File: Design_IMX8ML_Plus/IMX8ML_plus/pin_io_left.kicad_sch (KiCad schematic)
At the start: 2 parts, among them J1 DF40C-100DP-0.4V_51_, J2 DF40C-100DP-0.4V_51_

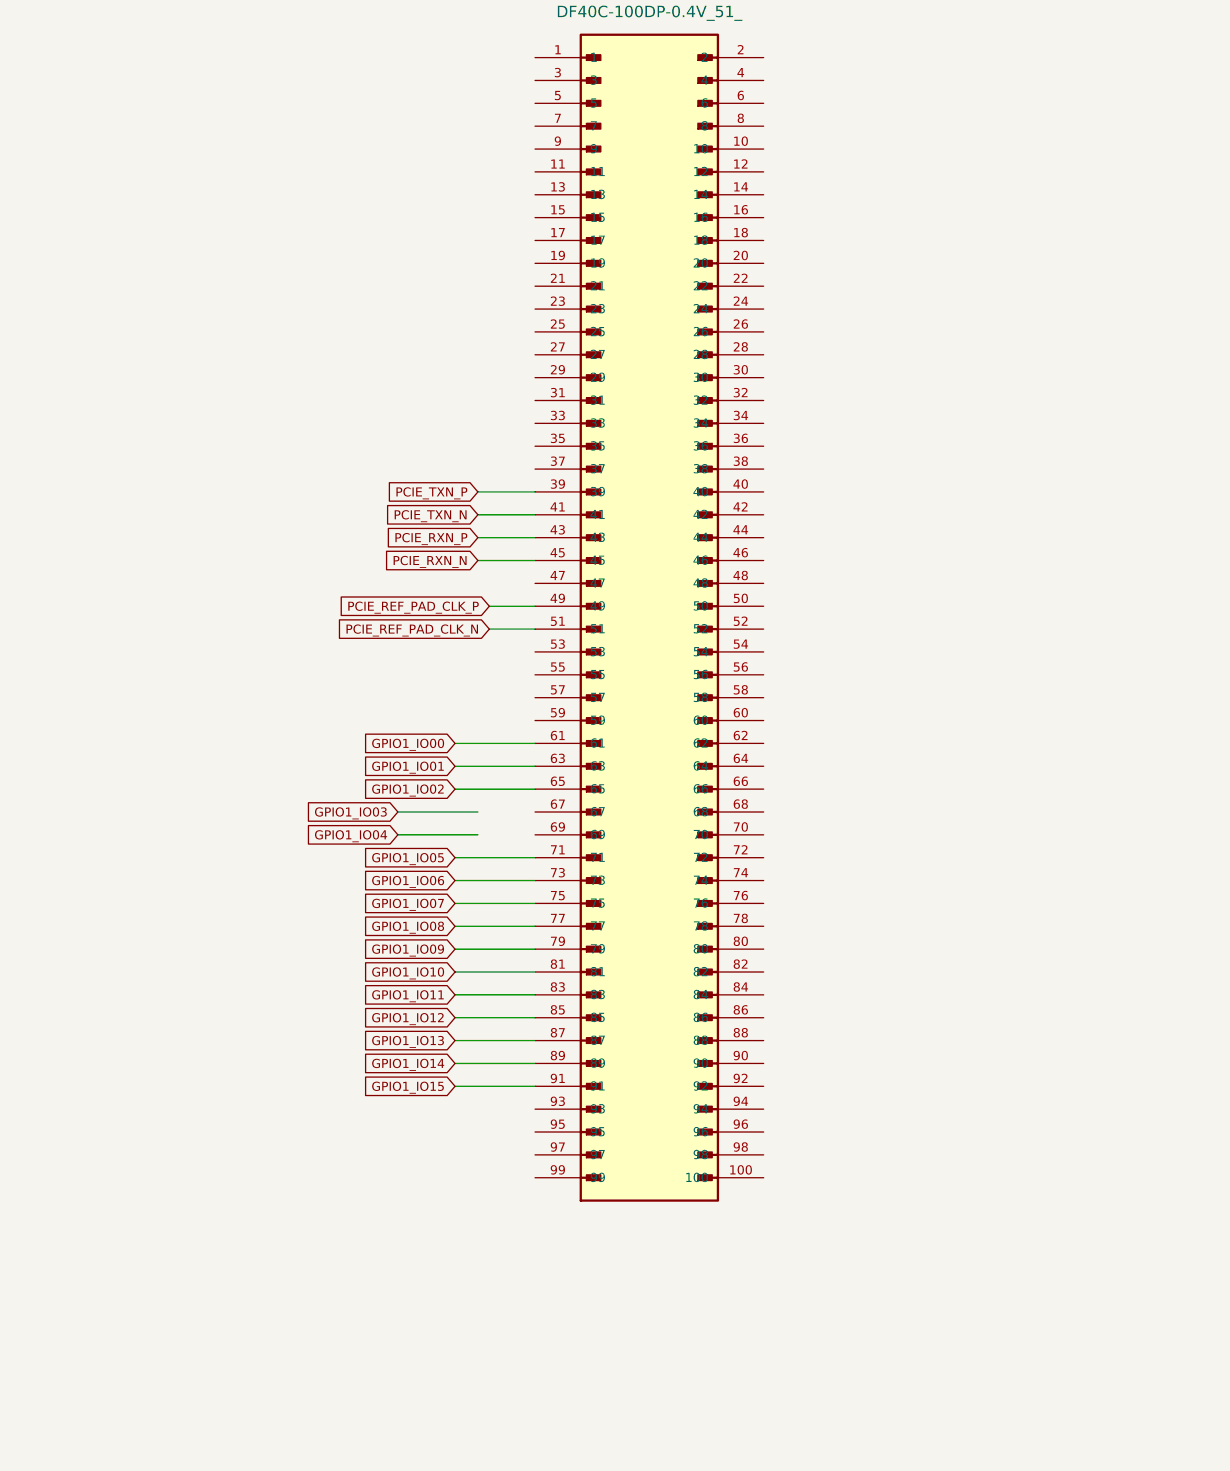
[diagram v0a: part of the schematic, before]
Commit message: Add power layer
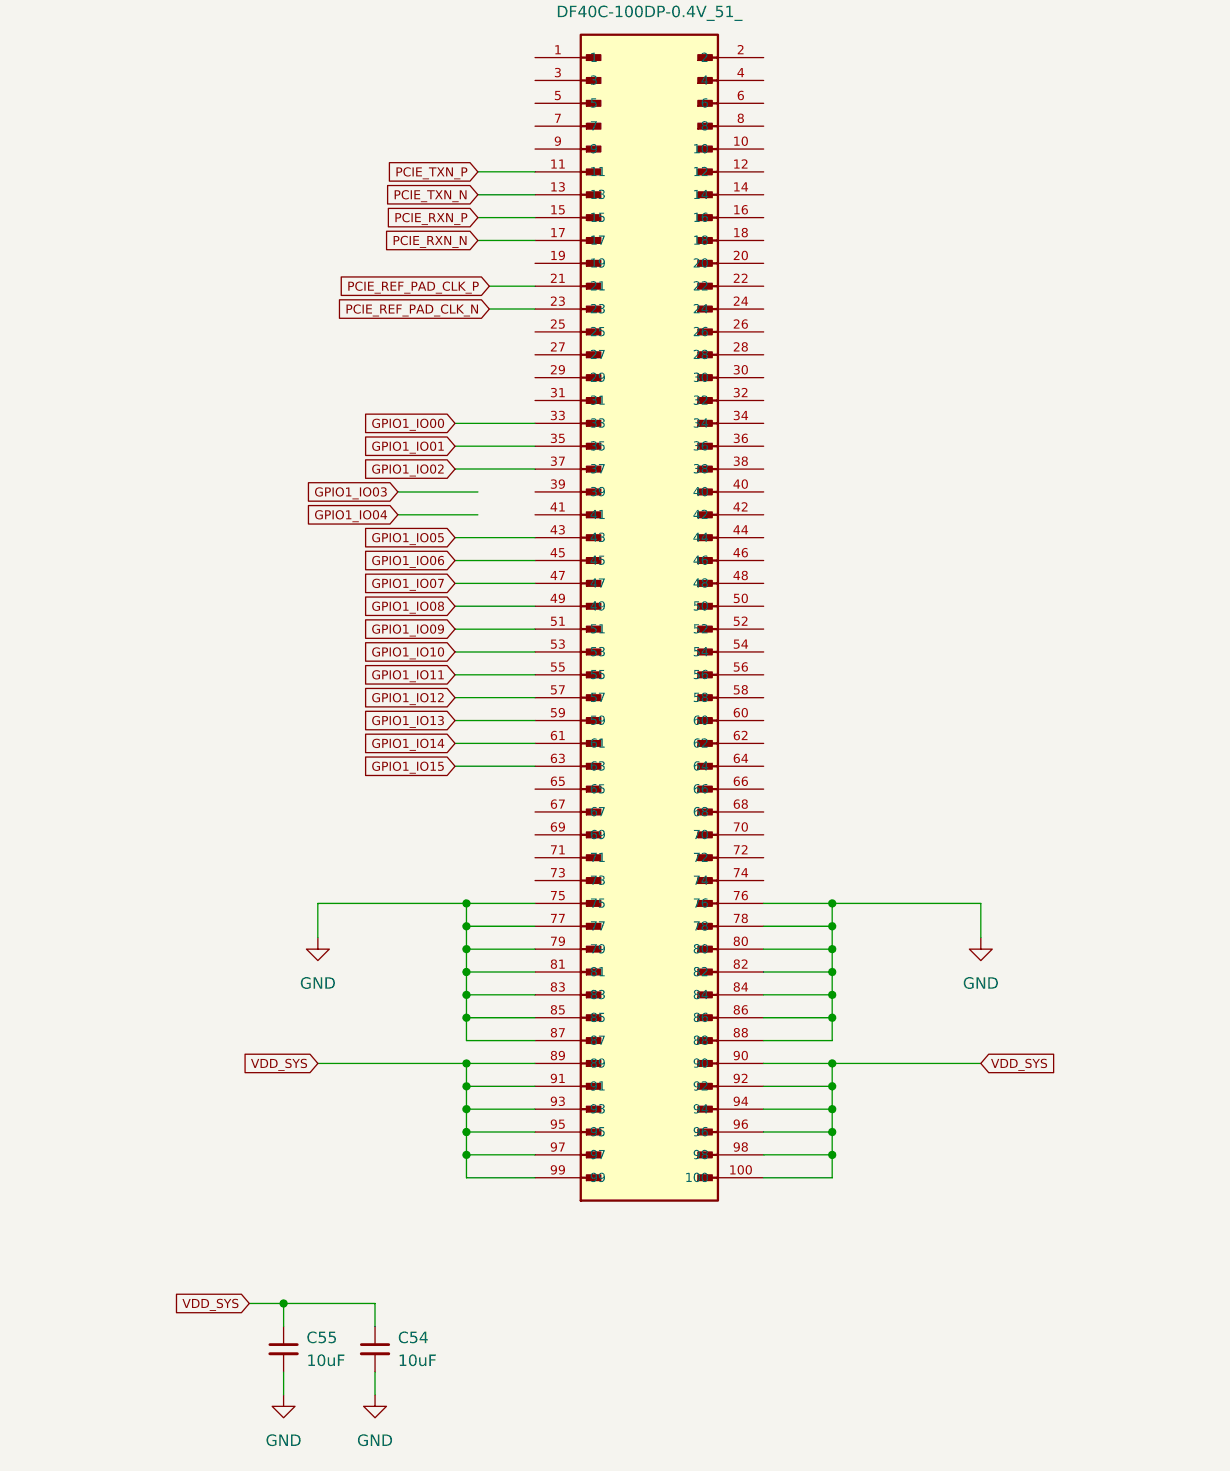
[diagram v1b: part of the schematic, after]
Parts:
- added C54, C55: 10uF, Capacitor_SMD:C_0201_0603Metric_Pad0.64x0.40mm_HandSolder, symbol Device:C_Small
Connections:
- net GPIO1_IO00: now also J1.33; no longer J1.61
- net GPIO1_IO01: now also J1.35; no longer J1.63
- net GPIO1_IO02: now also J1.37; no longer J1.65
- net GPIO1_IO05: now also J1.43; no longer J1.71
- net GPIO1_IO06: now also J1.45; no longer J1.73
- net GPIO1_IO07: now also J1.47; no longer J1.75
- net GPIO1_IO08: now also J1.49; no longer J1.77
- net GPIO1_IO09: now also J1.51; no longer J1.79
- net GPIO1_IO10: now also J1.53; no longer J1.81
- net GPIO1_IO11: now also J1.55; no longer J1.83
- net GPIO1_IO12: now also J1.57; no longer J1.85
- net GPIO1_IO13: now also J1.59; no longer J1.87
- net GPIO1_IO14: now also J1.61; no longer J1.89
- net GPIO1_IO15: now also J1.63; no longer J1.91
- net PCIE_REF_PAD_CLK_N: now also J1.23; no longer J1.51
- net PCIE_REF_PAD_CLK_P: now also J1.21; no longer J1.49
- net PCIE_RXN_N: now also J1.17; no longer J1.45
- net PCIE_RXN_P: now also J1.15; no longer J1.43
- net PCIE_TXN_N: now also J1.13; no longer J1.41
- net PCIE_TXN_P: now also J1.11; no longer J1.39
- net VDD_SYS: now reaches J1.100
- net VDD_SYS: now also J1.89, J1.90, J1.91, J1.92, J1.93, J1.94, J1.95, J1.96, J1.97, J1.98, J1.99, C54.1, C55.1
- net GND: now reaches J1.76
- net GND: now also J1.75, J1.77, J1.78, J1.79, J1.80, J1.81, J1.82, J1.83, J1.84, J1.85, J1.86, J1.87, J1.88, C54.2, C55.2

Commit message: Add SPB228 WIFI/BLE module
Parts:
- renumbered C54 to C10, C55 to C9

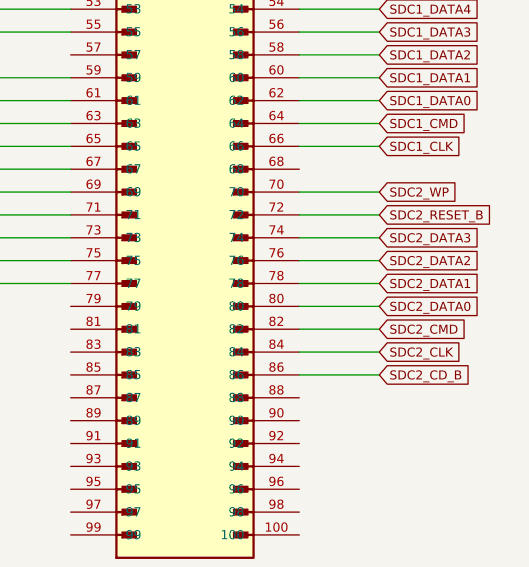
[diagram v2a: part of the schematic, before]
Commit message: Improve power source module in the base board
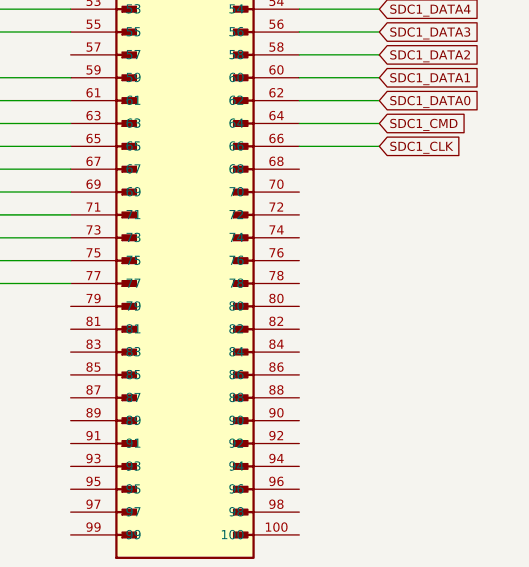
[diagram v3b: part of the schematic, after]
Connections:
- net SDC2_CD_B: no longer names the net of J2.86
- net SDC2_CLK: no longer names the net of J2.84
- net SDC2_CMD: no longer names the net of J2.82
- net SDC2_DATA0: no longer names the net of J2.80
- net SDC2_DATA1: no longer names the net of J2.78
- net SDC2_DATA2: no longer names the net of J2.76
- net SDC2_DATA3: no longer names the net of J2.74
- net SDC2_RESET_B: no longer names the net of J2.72
- net SDC2_WP: no longer names the net of J2.70

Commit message: CPU Board actualizate
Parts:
- J1: value DF40C-100DP-0.4V_51_ -> Back_Right
- J2: value DF40C-100DP-0.4V_51_ -> Front_Right
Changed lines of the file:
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@@
 			)
 		)
-		(property "Value" "DF40C-100DP-0.4V_51_"
+		(property "Value" "Front_Right"
 			(at 219.71 27.94 0)
 			(effects
@@
 			)
 		)
-		(property "Value" "DF40C-100DP-0.4V_51_"
+		(property "Value" "Back_Right"
 			(at 74.93 31.75 0)
 			(effects

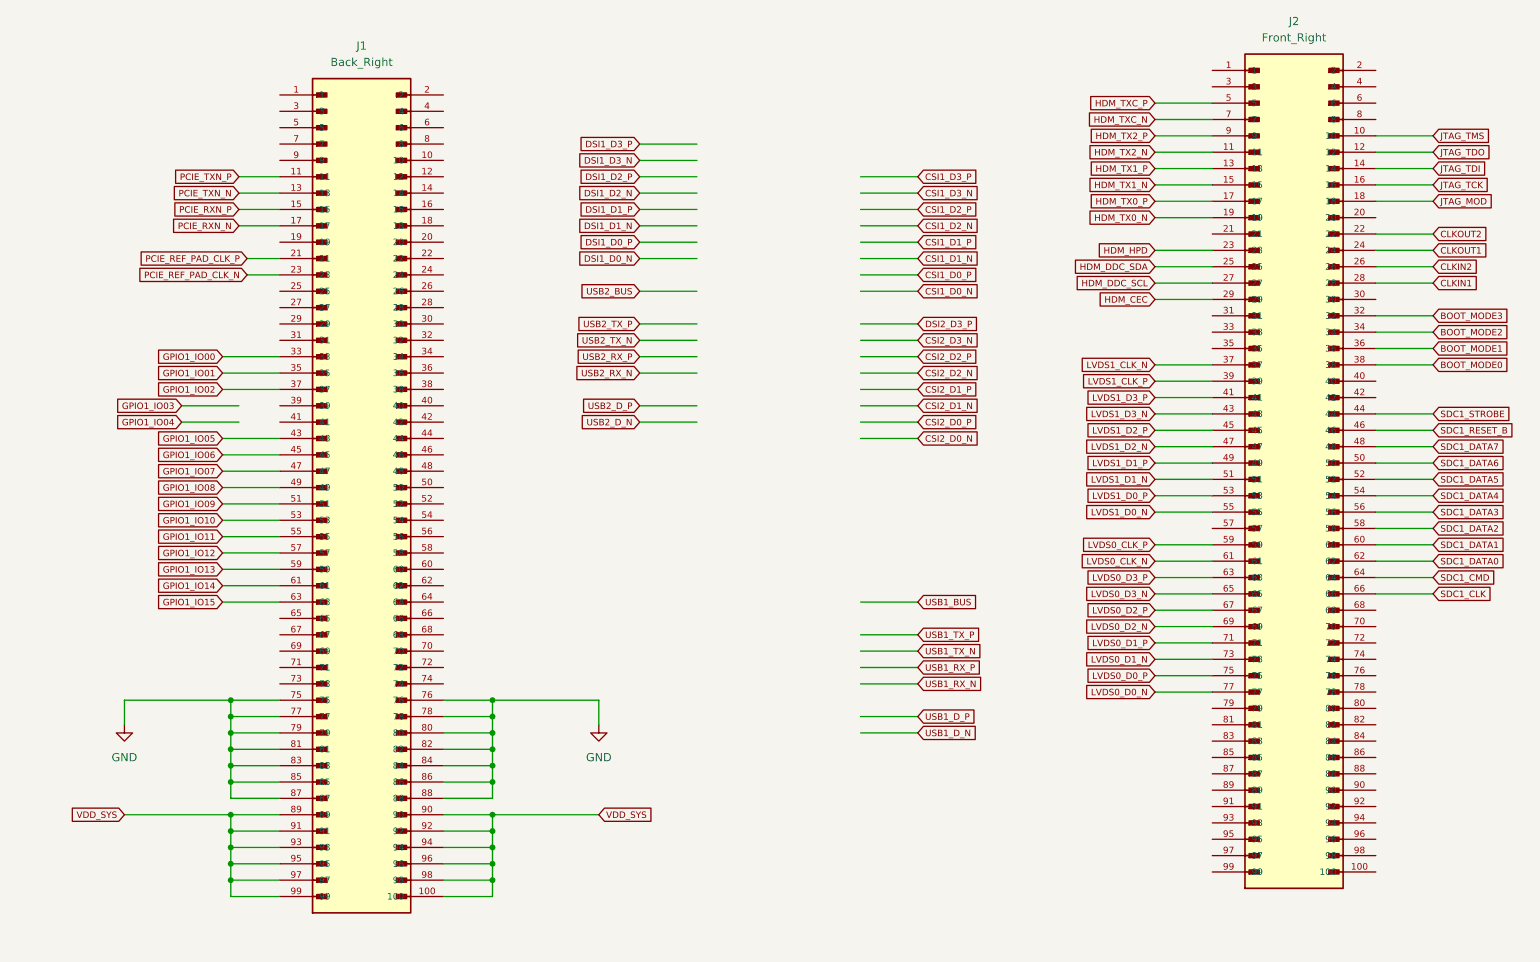
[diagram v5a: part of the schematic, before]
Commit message: [IMX8ML-Processor] Reorganization of the pinout conector since processor to conectors
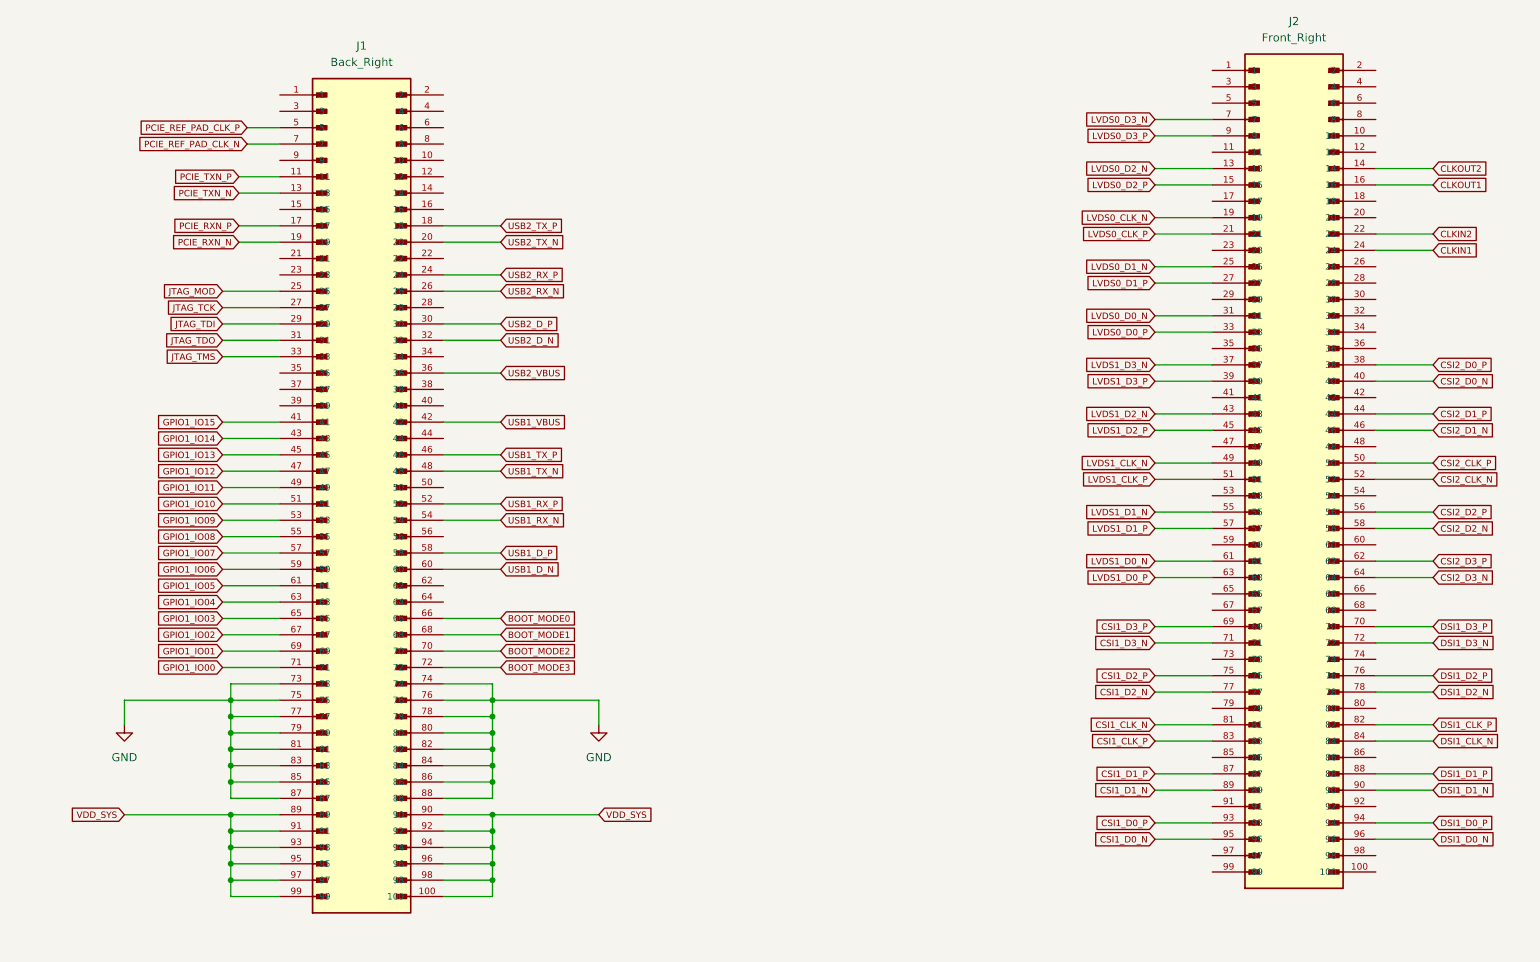
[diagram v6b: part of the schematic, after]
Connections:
- net HDM_DDC_SCL is gone; now on net LVDS0_D1_P: J2.27
- net HDM_DDC_SDA is gone; now on net LVDS0_D1_N: J2.25
- net HDM_TX0_N is gone; now on net LVDS0_CLK_N: J2.19
- net HDM_TX1_N is gone; now on net LVDS0_D2_P: J2.15
- net HDM_TX1_P is gone; now on net LVDS0_D2_N: J2.13
- net HDM_TX2_P is gone; now on net LVDS0_D3_P: J2.9
- net HDM_TXC_N is gone; now on net LVDS0_D3_N: J2.7
- net SDC1_CMD is gone; now on net CSI2_D3_N: J2.64
- net SDC1_DATA2 is gone; now on net CSI2_D2_N: J2.58
- net SDC1_DATA3 is gone; now on net CSI2_D2_P: J2.56
- net SDC1_RESET_B is gone; now on net CSI2_D1_N: J2.46
- net SDC1_STROBE is gone; now on net CSI2_D1_P: J2.44
- net BOOT_MODE0: now also J1.66; no longer J2.38
- net BOOT_MODE1: now also J1.68; no longer J2.36
- net BOOT_MODE2: now also J1.70; no longer J2.34
- net BOOT_MODE3: now also J1.72; no longer J2.32
- net CLKIN1: now also J2.24; no longer J2.28
- net CLKIN2: now also J2.22; no longer J2.26
- net CLKOUT1: now also J2.16; no longer J2.24
- net CLKOUT2: now also J2.14; no longer J2.22
- net CSI1_D0_N: now also J2.95
- net CSI1_D0_P: now also J2.93
- net CSI1_D1_N: now also J2.89
- net CSI1_D1_P: now also J2.87
- net CSI1_D2_N: now also J2.77
- net CSI1_D2_P: now also J2.75
- net CSI1_D3_N: now also J2.71
- net CSI1_D3_P: now also J2.69
- net CSI2_D0_N: now also J2.40
- net CSI2_D0_P: now also J2.38
- net DSI1_D0_N: now also J2.96
- net DSI1_D0_P: now also J2.94
- net DSI1_D1_N: now also J2.90
- net DSI1_D1_P: now also J2.88
- net DSI1_D2_N: now also J2.78
- net DSI1_D2_P: now also J2.76
- net DSI1_D3_N: now also J2.72
- net DSI1_D3_P: now also J2.70
- net GND: now also J1.73, J1.74
- net GPIO1_IO00: now also J1.71; no longer J1.33
- net GPIO1_IO01: now also J1.69; no longer J1.35
- net GPIO1_IO02: now also J1.67; no longer J1.37
- net GPIO1_IO03: now also J1.65
- net GPIO1_IO04: now also J1.63
- net GPIO1_IO05: now also J1.61; no longer J1.43
- net GPIO1_IO06: now also J1.59; no longer J1.45
- net GPIO1_IO07: now also J1.57; no longer J1.47
- net GPIO1_IO08: now also J1.55; no longer J1.49
- net GPIO1_IO09: now also J1.53; no longer J1.51
- net GPIO1_IO10: now also J1.51; no longer J1.53
- net GPIO1_IO11: now also J1.49; no longer J1.55
- net GPIO1_IO12: now also J1.47; no longer J1.57
- net GPIO1_IO13: now also J1.45; no longer J1.59
- net GPIO1_IO14: now also J1.43; no longer J1.61
- net GPIO1_IO15: now also J1.41; no longer J1.63
- net JTAG_MOD: now also J1.25; no longer J2.18
- net JTAG_TCK: now also J1.27; no longer J2.16
- net JTAG_TDI: now also J1.29; no longer J2.14
- net JTAG_TDO: now also J1.31; no longer J2.12
- net JTAG_TMS: now also J1.33; no longer J2.10
- net LVDS0_CLK_N: no longer J2.61
- net LVDS0_CLK_P: now also J2.21; no longer J2.59
- net LVDS0_D0_N: now also J2.31; no longer J2.77
- net LVDS0_D0_P: now also J2.33; no longer J2.75
- net LVDS0_D1_N: no longer J2.73
- net LVDS0_D1_P: no longer J2.71
- net LVDS0_D2_N: no longer J2.69
- net LVDS0_D2_P: no longer J2.67
- net LVDS0_D3_N: no longer J2.65
- net LVDS0_D3_P: no longer J2.63
- net LVDS1_CLK_N: now also J2.49; no longer J2.37
- net LVDS1_CLK_P: now also J2.51; no longer J2.39
- net LVDS1_D0_N: now also J2.61; no longer J2.55
- net LVDS1_D0_P: now also J2.63; no longer J2.53
- net LVDS1_D1_N: now also J2.55; no longer J2.51
- net LVDS1_D1_P: now also J2.57; no longer J2.49
- net LVDS1_D2_N: now also J2.43; no longer J2.47
- net LVDS1_D3_N: now also J2.37; no longer J2.43
- net LVDS1_D3_P: now also J2.39; no longer J2.41
- net PCIE_REF_PAD_CLK_N: now also J1.7; no longer J1.23
- net PCIE_REF_PAD_CLK_P: now also J1.5; no longer J1.21
- net PCIE_RXN_N: now also J1.19; no longer J1.17
- net PCIE_RXN_P: now also J1.17; no longer J1.15
- net USB1_D_N: now also J1.60
- net USB1_D_P: now also J1.58
- net USB1_RX_N: now also J1.54
- net USB1_RX_P: now also J1.52
- net USB1_TX_N: now also J1.48
- net USB1_TX_P: now also J1.46
- net USB2_D_N: now also J1.32
- net USB2_D_P: now also J1.30
- net USB2_RX_N: now also J1.26
- net USB2_RX_P: now also J1.24
- net USB2_TX_N: now also J1.20
- net USB2_TX_P: now also J1.18
- net CSI1_CLK_N: now reaches J2.81
- net DSI1_CLK_P: now reaches J2.82
- net CSI1_CLK_P: now reaches J2.83
- net DSI1_CLK_N: now reaches J2.84
- net USB2_VBUS: now reaches J1.36
- net USB1_VBUS: now reaches J1.42
- net HDM_CEC: no longer names the net of J2.29
- net HDM_HPD: no longer names the net of J2.23
- net HDM_TX0_P: no longer names the net of J2.17
- net HDM_TX2_N: no longer names the net of J2.11
- net HDM_TXC_P: no longer names the net of J2.5
- net SDC1_CLK: no longer names the net of J2.66
- net SDC1_DATA0 renamed CSI2_D3_P
- net SDC1_DATA1: no longer names the net of J2.60
- net SDC1_DATA4: no longer names the net of J2.54
- net SDC1_DATA5 renamed CSI2_CLK_N
- net SDC1_DATA6 renamed CSI2_CLK_P
- net SDC1_DATA7: no longer names the net of J2.48
